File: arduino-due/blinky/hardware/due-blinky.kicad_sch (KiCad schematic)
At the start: 4 parts, among them J1 2x5 1.27 mm, on board, J2 2x5 1.27 mm, 3.3 V capable

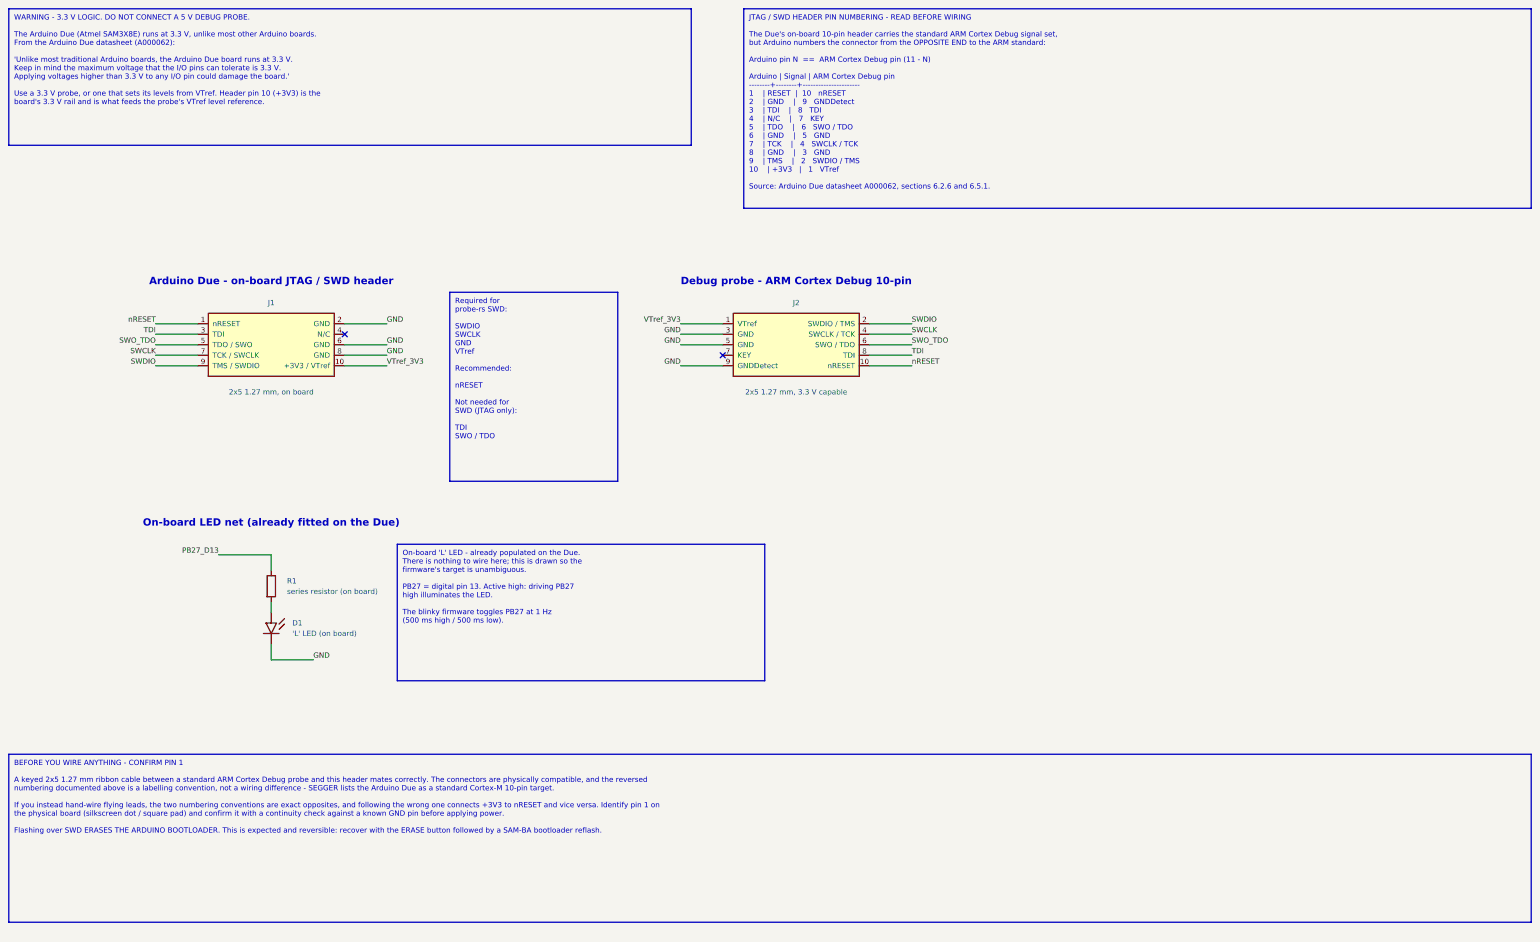
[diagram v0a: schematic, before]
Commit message: story(issue-3): blink an external LED on PB26/D22, not the on-board one
An on-board D13 LED blinking is weak evidence that the firmware is
working. Bootloader activity or a watchdog reset loop can make the board
blink on its own, and issue #3 calls out that exact failure mode: with
the watchdog left enabled the board resets every few seconds and "the
blink looks like a boot loop". By eye, that is indistinguishable from a
correct 1 Hz blink on D13.

Move the indicator to an externally wired LED on PB26 (digital pin 22),
which per the Arduino variant table has no on-board LED, no boot-time
role, and no peripheral alternate function. If it blinks at a steady
1 Hz, the firmware is running and toggling a pin.

Two hardware details verified from primary sources rather than assumed,
both of which are easy to get wrong:

- PB26 is in the SAM3X datasheet's Group 2 (PB[25-31]), whose source
  limit is IOH = -3 mA at VOH = VDDIO - 0.4 V, not the -15 mA that
  Group 1 pins allow. The reflexive 220 ohm would draw roughly 4 mA and
  sit outside that spec, so R1 is 1 k (about 1 mA) with 470 ohm noted as
  the practical floor.

- D22 is the second pin on the D22-D53 even-numbered row, and the pin
  immediately beside it is +5V. Miscounting by one position feeds 5 V
  into a board whose I/O pins tolerate 3.3 V, so the sheet spells out
  the positions and says to confirm GND with a continuity check.

Refs #3

Co-Authored-By: Claude Opus 4.8 <noreply@anthropic.com>
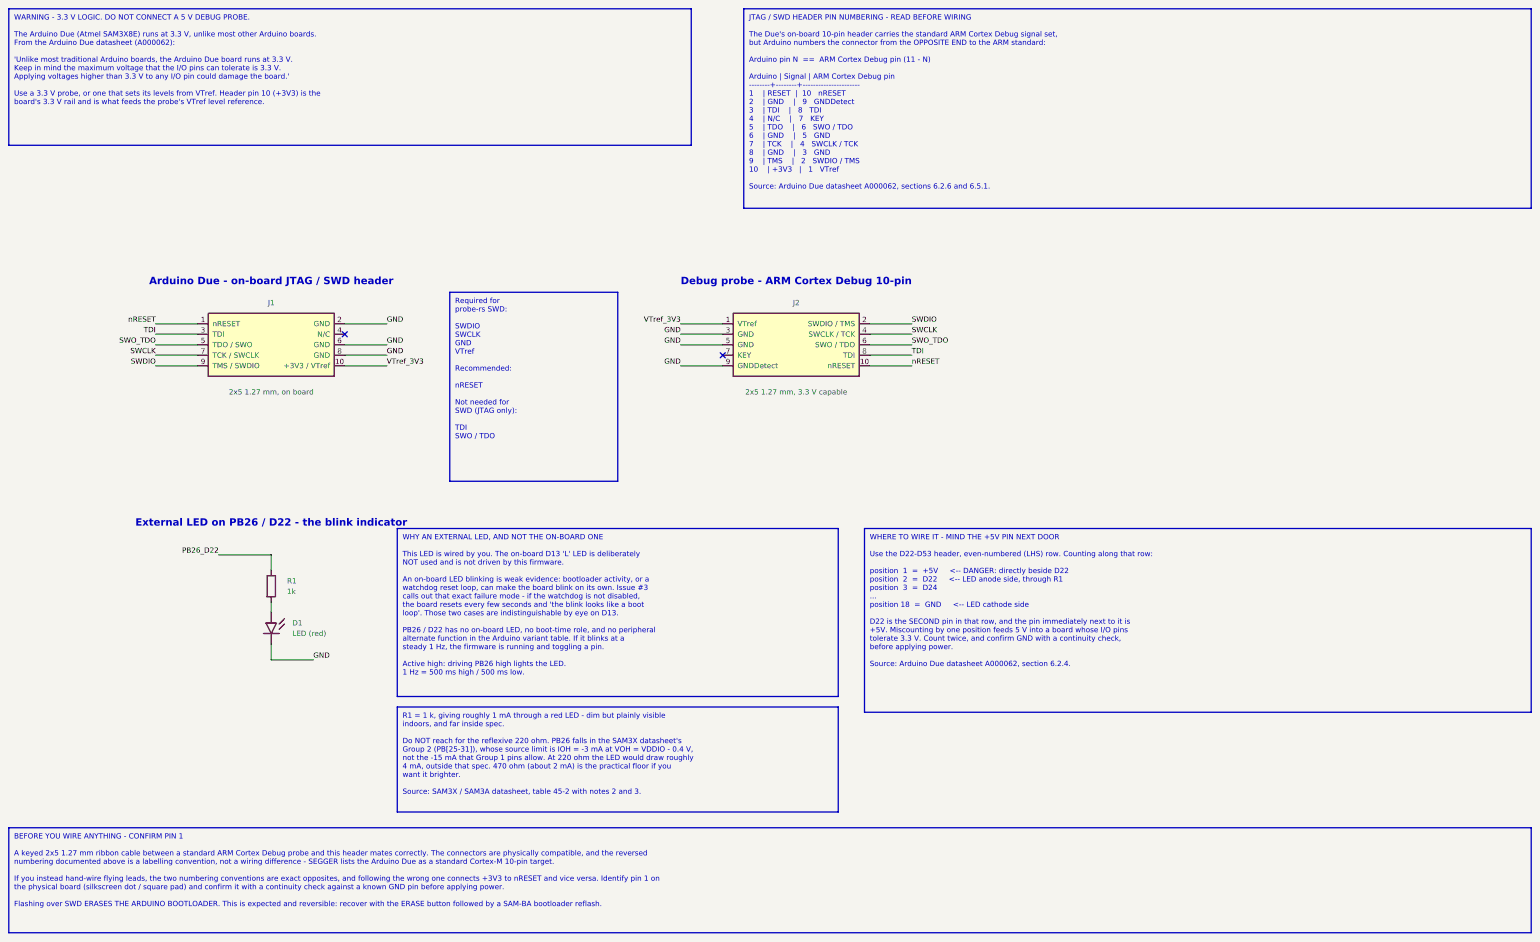
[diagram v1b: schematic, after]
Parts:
- D1: value 'L' LED (on board) -> LED (red)
- R1: value series resistor (on board) -> 1k
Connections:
- net PB27_D13 renamed PB26_D22
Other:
- note added: "External LED on PB26 / D22 - the blink indicator"
- note removed: "On-board LED net (already fitted on the Due)"
- title: Arduino Due blinky - SWD wiring and on-board LED -> Arduino Due blinky - SWD wiring and external LED
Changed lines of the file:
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@@
 	(paper "A3")
 	(title_block
-		(title "Arduino Due blinky - SWD wiring and on-board LED")
+		(title "Arduino Due blinky - SWD wiring and external LED")
 		(date "2026-07-19")
 		(rev "1")
@@
 		)
 	)
-	(text_box "On-board 'L' LED - already populated on the Due.\nThere is nothing to wire here; this is drawn so the\nfirmware's target is unambiguous.\n\nPB27 = digital pin 13. Active high: driving PB27\nhigh illuminates the LED.\n\nThe blinky firmware toggles PB27 at 1 Hz\n(500 ms high / 500 ms low)."
-		(exclude_from_sim no)
-		(at 119.38 149.86 0)
-		(size 88.9 33.02)
+	(text_box "WHY AN EXTERNAL LED, AND NOT THE ON-BOARD ONE\n\nThis LED is wired by you. The on-board D13 'L' LED is deliberately\nNOT used and is not driven by this firmware.\n\nAn on-board LED blinking is weak evidence: bootloader activity, or a\nwatchdog reset loop, can make the board blink on its own. Issue #3\ncalls out that exact failure mode - if the watchdog is not disabled,\nthe board resets every few seconds and 'the blink looks like a boot\nloop'. Those two cases are indistinguishable by eye on D13.\n\nPB26 / D22 has no on-board LED, no boot-time role, and no peripheral\nalternate function in the Arduino variant table. If it blinks at a\nsteady 1 Hz, the firmware is running and toggling a pin.\n\nActive high: driving PB26 high lights the LED.\n1 Hz = 500 ms high / 500 ms low."
+		(exclude_from_sim no)
+		(at 119.38 146.05 0)
+		(size 106.68 40.64)
 		(margins 1.27 1.27 1.27 1.27)
 		(stroke
@@
 		)
 	)
+	(text_box "WHERE TO WIRE IT - MIND THE +5V PIN NEXT DOOR\n\nUse the D22-D53 header, even-numbered (LHS) row. Counting along that row:\n\n     position  1  =  +5V     <-- DANGER: directly beside D22\n     position  2  =  D22     <-- LED anode side, through R1\n     position  3  =  D24\n        ...\n     position 18  =  GND     <-- LED cathode side\n\nD22 is the SECOND pin in that row, and the pin immediately next to it is\n+5V. Miscounting by one position feeds 5 V into a board whose I/O pins\ntolerate 3.3 V. Count twice, and confirm GND with a continuity check,\nbefore applying power.\n\nSource: Arduino Due datasheet A000062, section 6.2.4."
+		(exclude_from_sim no)
+		(at 232.41 146.05 0)
+		(size 161.29 44.45)
+		(margins 1.27 1.27 1.27 1.27)
+		(stroke
+			(width 0.254)
+			(type default)
+		)
+		(fill
+			(type color)
+			(color 255 214 214 1)
+		)
+		(effects
+			(font
+				(size 1.27 1.27)
+			)
+			(justify left top)
+		)
+	)
+	(text_box "R1 = 1 k, giving roughly 1 mA through a red LED - dim but plainly visible\nindoors, and far inside spec.\n\nDo NOT reach for the reflexive 220 ohm. PB26 falls in the SAM3X datasheet's\nGroup 2 (PB[25-31]), whose source limit is IOH = -3 mA at VOH = VDDIO - 0.4 V,\nnot the -15 mA that Group 1 pins allow. At 220 ohm the LED would draw roughly\n4 mA, outside that spec. 470 ohm (about 2 mA) is the practical floor if you\nwant it brighter.\n\nSource: SAM3X / SAM3A datasheet, table 45-2 with notes 2 and 3."
+		(exclude_from_sim no)
+		(at 119.38 189.23 0)
+		(size 106.68 25.4)
+		(margins 1.27 1.27 1.27 1.27)
+		(stroke
+			(width 0.254)
+			(type default)
+		)
+		(fill
+			(type color)
+			(color 255 249 214 1)
+		)
+		(effects
+			(font
+				(size 1.27 1.27)
+			)
+			(justify left top)
+		)
+	)
 	(text_box "BEFORE YOU WIRE ANYTHING - CONFIRM PIN 1\n\nA keyed 2x5 1.27 mm ribbon cable between a standard ARM Cortex Debug probe and this header mates correctly. The connectors are physically compatible, and the reversed\nnumbering documented above is a labelling convention, not a wiring difference - SEGGER lists the Arduino Due as a standard Cortex-M 10-pin target.\n\nIf you instead hand-wire flying leads, the two numbering conventions are exact opposites, and following the wrong one connects +3V3 to nRESET and vice versa. Identify pin 1 on\nthe physical board (silkscreen dot / square pad) and confirm it with a continuity check against a known GND pin before applying power.\n\nFlashing over SWD ERASES THE ARDUINO BOOTLOADER. This is expected and reversible: recover with the ERASE button followed by a SAM-BA bootloader reflash."
 		(exclude_from_sim no)
-		(at 25.4 200.66 0)
-		(size 368.3 40.64)
+		(at 25.4 218.44 0)
+		(size 368.3 25.4)
 		(margins 1.27 1.27 1.27 1.27)
 		(stroke
@@
 		)
 	)
-	(label "PB27_D13"
+	(label "PB26_D22"
 		(at 76.2 152.4 0)
 		(effects
@@
 		)
 	)
-	(text "On-board LED net (already fitted on the Due)"
+	(text "External LED on PB26 / D22 - the blink indicator"
 		(exclude_from_sim no)
 		(at 88.9 144.78 0)
@@
 			)
 		)
-		(property "Value" "series resistor (on board)"
+		(property "Value" "1k"
 			(at 92.71 161.29 0)
 			(effects
@@
 			)
 		)
-		(property "Value" "'L' LED (on board)"
+		(property "Value" "LED (red)"
 			(at 93.98 171.45 0)
 			(effects
